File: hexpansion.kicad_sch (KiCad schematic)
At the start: 7 parts, among them J1 Hexpansion-Connector, J2 Conn_02x10_Odd_Even

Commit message: extract out hexpansion parts to custom library
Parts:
- J1: footprint tildagon:hexpansion-edge-connector -> parts:hexpansion-edge-connector; symbol tildagon:hexpansion-edge-connector -> parts:hexpansion-edge-connector
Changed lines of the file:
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@@
 	)
 	(symbol
-		(lib_id "tildagon:hexpansion-edge-connector")
+		(lib_id "parts:hexpansion-edge-connector")
 		(at 83.82 74.93 0)
 		(unit 1)
-		(exclude_from_sim yes)
+		(exclude_from_sim no)
 		(in_bom no)
 		(on_board yes)
@@
 			)
 		)
-		(property "Footprint" "tildagon:hexpansion-edge-connector"
+		(property "Footprint" "parts:hexpansion-edge-connector"
 			(at 83.82 77.47 0)
 			(effects

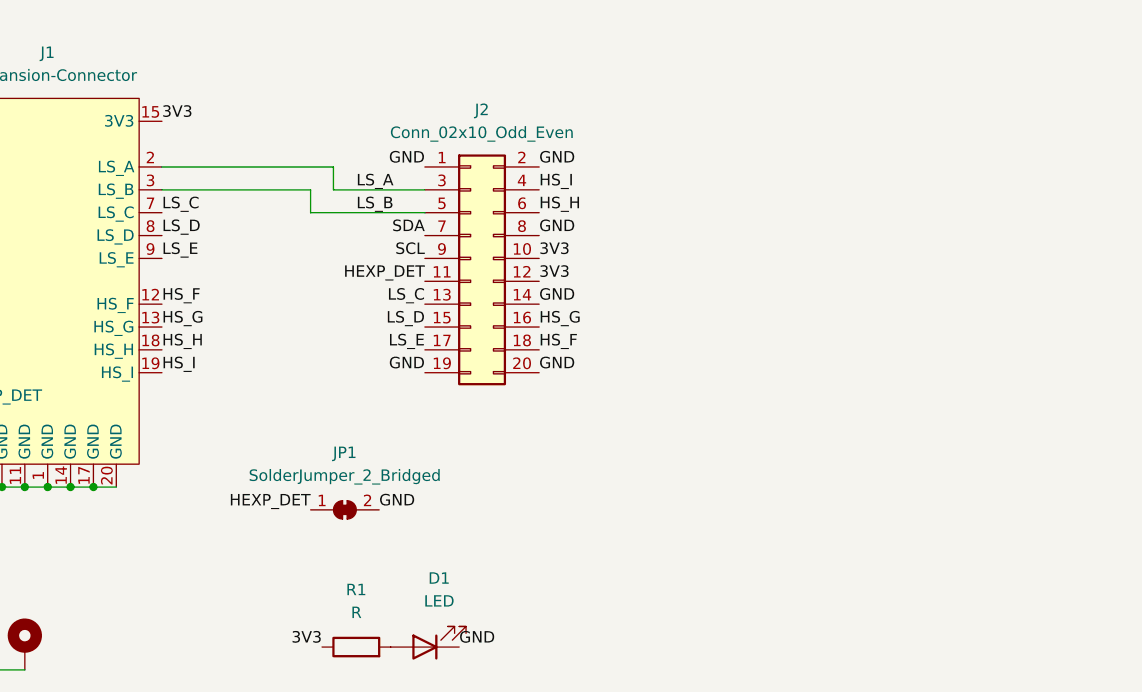
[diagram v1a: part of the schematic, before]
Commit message: add codec symbol
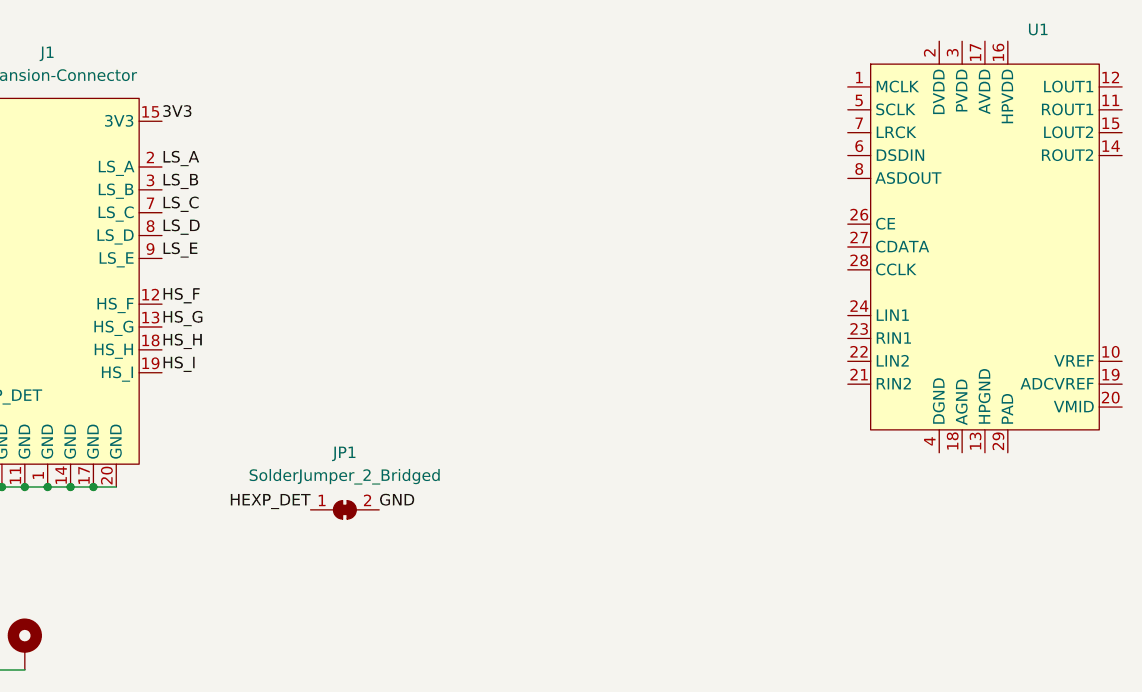
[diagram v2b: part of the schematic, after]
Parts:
- removed D1: LED, LED_SMD:LED_0805_2012Metric, symbol Device:LED
- removed J2: Conn_02x10_Odd_Even, Connector_PinHeader_2.54mm:PinHeader_2x10_P2.54mm_Vertical, symbol Connector_Generic:Conn_02x10_Odd_Even
- removed R1: R, Resistor_SMD:R_0603_1608Metric, symbol Device:R
- added U1: ~, symbol parts:ES8388

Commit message: rough sch
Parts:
- added C1, C10, C2, C4, C6, C8: 10 uF, symbol Device:C_Small
- added C11, C12, C21, C3, C5, C7, C9: 0.1 uF, symbol Device:C_Small
- added C13, C14: 47 uF, symbol Device:C_Small
- added C15, C16, C17, C18, C19, C20: 1 uF, symbol Device:C_Small
- added J2, J3, J4: AudioJack4, symbol Connector_Audio:AudioJack4
- added JP2: ADDR_LSB0, symbol Jumper:SolderJumper_3_Bridged12
- added R1, R2, R3, R4: 10, symbol Device:R_Small
- added R5, R6, R7, R8: 10k, symbol Device:R_Small
- added TP1: TestPoint, symbol Connector:TestPoint
- added U2, U3: 74LVC1G125, symbol 74xGxx:74LVC1G125
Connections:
- net 3V3 is gone; now on net +3.3V: J1.15 (3V3), J1.16 (3V3)
- net HS_F is gone; now on net MCLK: J1.12 (HS_F)
- net HS_G is gone; now on net SCLK: J1.13 (HS_G)
- net HS_H is gone; now on net LRCLK: J1.18 (HS_H)
- net GND: now also U1.13 (HPGND), U1.18 (AGND), U1.29 (PAD), U1.4 (DGND), C1.2, C10.2, C11.2, C12.2, C2.2, C21.2, C3.2, C4.2, C5.2, C6.2, C7.2, C8.2, C9.2, J2.R2, J3.R2, J3.S, J4.R2, J4.S, JP2.1 (A), R8.2, U2.3 (GND), U3.3 (GND)
- net SCL: now also U1.28 (CCLK), R6.2
- net SDA: now also U1.27 (CDATA), R5.2
- net MCLK: now reaches U1.1 (MCLK)
- net at U1.10 (VREF): now also C1.1
- net at U1.11 (ROUT1): now also C14.1
- net at U1.12 (LOUT1): now also C13.1
- net at U1.14 (ROUT2): now also C16.1
- net at U1.15 (LOUT2): now also C15.1
- net +3.3V: now reaches U1.16 (HPVDD)
- net +3.3V: now also U1.17 (AVDD), U1.2 (DVDD), U1.3 (PVDD), C10.1, C11.1, C12.1, C21.1, C6.1, C7.1, C8.1, C9.1, JP2.3 (B), R5.1, R6.1, R7.1, U2.5 (VCC), U3.5 (VCC)
- net at U1.19 (ADCVREF): now also C2.1, C3.1
- net at U1.20 (VMID): now also C4.1, C5.1
- net at U1.21 (RIN2): now also C20.2
- net at U1.22 (LIN2): now also C19.2
- net at U1.23 (RIN1): now also C18.2
- net at U1.24 (LIN1): now also C17.2
- net at U1.26 (CE): now also JP2.2 (C)
- net SCLK: now reaches U1.5 (SCLK)
- net DSDIN: now reaches U1.6 (DSDIN)
- net DSDIN: now also U3.4
- net LRCLK: now reaches U1.7 (LRCK)
- net ASDOUT: now reaches U1.8 (ASDOUT)
- net ASDOUT: now also U2.2
- net HS_I renamed I2S_DATA_SHARED
- net I2S_DATA_SHARED: now also U2.4, U3.2
- net LS_A renamed ~{MIC_EN}
- net ~{MIC_EN}: now also R7.2, U2.1
- net LS_B renamed ~{OUT_EN}
- net ~{OUT_EN}: now also R8.1, U3.1
- net LS_C: no longer names the net of J1.7 (LS_C)
- net LS_D: no longer names the net of J1.8 (LS_D)
- net LS_E: no longer names the net of J1.9 (LS_E)
- new net: C13.2, R1.1
- new net: C14.2, R2.1
- new net: C15.2, R4.1
- new net: C16.2, R3.1
- new net HP_L: J2.T, R1.2
- new net HP_R: J2.R1, R2.2
- new net LINEIN_L: C19.1, J4.T
- new net LINEIN_R: C20.1, J4.R1
- new net LINEOUT_L: J3.T, R4.2
- new net LINEOUT_R: J3.R1, R3.2
- new net MIC_L: C17.1, J2.S
- new net MIC_R: C18.1, TP1.1
- no-connect marks 0 -> 3
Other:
- note added: "AVDD"
- note added: "DVDD"
- note added: "HPVDD"
- note added: "PVDD"
- note added: "TODO do we want higher quality filtering?"
- note added: "lol the cheapest jack is a TRRS"
- note added: "todo verify pin ordering"
- note added: "xxx verify this is a MCLK capable pin???"
- moved on the sheet: J1, JP1, U1

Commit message: rough everything
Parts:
- added TP2: SCL, TestPoint:TestPoint_Pad_2.0x2.0mm, symbol Connector:TestPoint
- added TP3: SDA, TestPoint:TestPoint_Pad_2.0x2.0mm, symbol Connector:TestPoint
- added TP4: ASDOUT, TestPoint:TestPoint_Pad_1.0x1.0mm, symbol Connector:TestPoint
- added TP5: DSDIN, TestPoint:TestPoint_Pad_1.0x1.0mm, symbol Connector:TestPoint
- C1, C10, C2, C4, C6, C8: footprint (none) -> Capacitor_SMD:C_0603_1608Metric
- C11, C12, C21, C3, C5, C7, C9: footprint (none) -> Capacitor_SMD:C_0402_1005Metric
- C13, C14, C15, C16, C17, C18, C19, C20: footprint (none) -> Capacitor_SMD:C_1206_3216Metric
- J2, J3, J4: footprint (none) -> Connector_Audio:Jack_3.5mm_PJ320D_Horizontal
- JP2: footprint (none) -> Jumper:SolderJumper-3_P1.3mm_Bridged12_RoundedPad1.0x1.5mm
- R1, R2, R3, R4: footprint (none) -> Resistor_SMD:R_0603_1608Metric
- R5, R6, R7, R8: footprint (none) -> Resistor_SMD:R_0402_1005Metric
- TP1: footprint (none) -> TestPoint:TestPoint_Pad_2.0x2.0mm
- U1: footprint (none) -> parts:QFN-28-1EP_4x4mm_P0.45mm_EP2.6x2.6mm
- U2, U3: footprint (none) -> Package_TO_SOT_SMD:SOT-23-5
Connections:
- net ASDOUT: now also TP4.1
- net DSDIN: now also TP5.1
- net SCL: now also TP2.1
- net SDA: now also TP3.1
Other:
- note added: "FIXME THIS FOOTPRINT IS WRONG!"
- moved on the sheet: R8

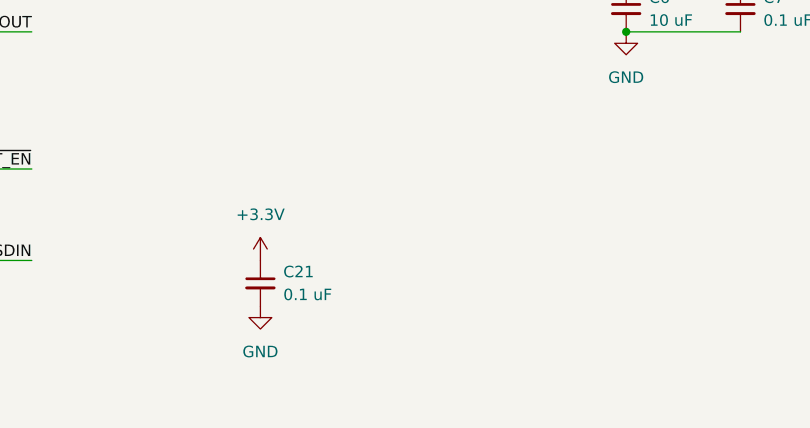
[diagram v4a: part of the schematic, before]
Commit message: rough route
purposely ignore extra gnd
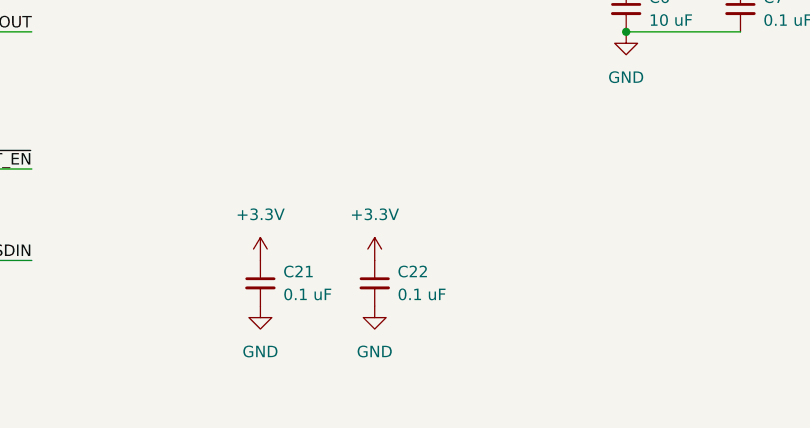
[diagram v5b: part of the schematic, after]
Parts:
- added C22: 0.1 uF, Capacitor_SMD:C_0402_1005Metric, symbol Device:C_Small
- J2, J3, J4: footprint Connector_Audio:Jack_3.5mm_PJ320D_Horizontal -> Connector_Audio:Jack_3.5mm_KoreanHropartsElec_PJ-320D-4A_Horizontal
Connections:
- net +3.3V: now also C22.1
- net GND: now also C22.2
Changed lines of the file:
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@@
 			)
 		)
-		(property "Footprint" "Connector_Audio:Jack_3.5mm_PJ320D_Horizontal"
+		(property "Footprint" "Connector_Audio:Jack_3.5mm_KoreanHropartsElec_PJ-320D-4A_Horizontal"
 			(at 182.88 25.4 0)
 			(effects
@@
 			)
 		)
-		(property "Footprint" "Connector_Audio:Jack_3.5mm_PJ320D_Horizontal"
+		(property "Footprint" "Connector_Audio:Jack_3.5mm_KoreanHropartsElec_PJ-320D-4A_Horizontal"
 			(at 144.78 25.4 0)
 			(effects
@@
 	)
 	(symbol
+		(lib_id "power:+3.3V")
+		(at 139.7 177.8 0)
+		(unit 1)
+		(exclude_from_sim no)
+		(in_bom yes)
+		(on_board yes)
+		(dnp no)
+		(fields_autoplaced yes)
+		(property "Reference" "#PWR028"
+			(at 139.7 181.61 0)
+			(effects
+				(font
+					(size 1.27 1.27)
+				)
+				(hide yes)
+			)
+		)
+		(property "Value" "+3.3V"
+			(at 139.7 172.72 0)
+			(effects
+				(font
+					(size 1.27 1.27)
+				)
+			)
+		)
+		(property "Footprint" ""
+			(at 139.7 177.8 0)
+			(effects
+				(font
+					(size 1.27 1.27)
+				)
+				(hide yes)
+			)
+		)
+		(property "Datasheet" ""
+			(at 139.7 177.8 0)
+			(effects
+				(font
+					(size 1.27 1.27)
+				)
+				(hide yes)
+			)
+		)
+		(property "Description" "Power symbol creates a global label with name \"+3.3V\""
+			(at 139.7 177.8 0)
+			(effects
+				(font
+					(size 1.27 1.27)
+				)
+				(hide yes)
+			)
+		)
+		(pin "1"
+		)
+		(instances
+			(project "hexpansion"
+				(path "/fb9bfa6e-c44d-469c-aa90-8ec28bcdf17f"
+					(reference "#PWR028")
+					(unit 1)
+				)
+			)
+		)
+	)
+	(symbol
 		(lib_id "power:GND")
 		(at 60.96 187.96 0)
@@
 	(symbol
 		(lib_id "Device:C_Small")
+		(at 139.7 180.34 0)
+		(unit 1)
+		(exclude_from_sim no)
+		(in_bom yes)
+		(on_board yes)
+		(dnp no)
+		(fields_autoplaced yes)
+		(property "Reference" "C22"
+			(at 142.24 179.0762 0)
+			(effects
+				(font
+					(size 1.27 1.27)
+				)
+				(justify left)
+			)
+		)
+		(property "Value" "0.1 uF"
+			(at 142.24 181.6162 0)
+			(effects
+				(font
+					(size 1.27 1.27)
+				)
+				(justify left)
+			)
+		)
+		(property "Footprint" "Capacitor_SMD:C_0402_1005Metric"
+			(at 139.7 180.34 0)
+			(effects
+				(font
+					(size 1.27 1.27)
+				)
+				(hide yes)
+			)
+		)
+		(property "Datasheet" "~"
+			(at 139.7 180.34 0)
+			(effects
+				(font
+					(size 1.27 1.27)
+				)
+				(hide yes)
+			)
+		)
+		(property "Description" "Unpolarized capacitor, small symbol"
+			(at 139.7 180.34 0)
+			(effects
+				(font
+					(size 1.27 1.27)
+				)
+				(hide yes)
+			)
+		)
+		(pin "1"
+		)
+		(pin "2"
+		)
+		(instances
+			(project "hexpansion"
+				(path "/fb9bfa6e-c44d-469c-aa90-8ec28bcdf17f"
+					(reference "C22")
+					(unit 1)
+				)
+			)
+		)
+	)
+	(symbol
+		(lib_id "Device:C_Small")
 		(at 111.76 109.22 90)
 		(unit 1)
@@
 			)
 		)
-		(property "Footprint" "Connector_Audio:Jack_3.5mm_PJ320D_Horizontal"
+		(property "Footprint" "Connector_Audio:Jack_3.5mm_KoreanHropartsElec_PJ-320D-4A_Horizontal"
 			(at 182.88 53.34 0)
 			(effects
@@
 					(unit 1)
 				)
+			)
+		)
+	)
+	(symbol
+		(lib_id "power:GND")
+		(at 139.7 182.88 0)
+		(unit 1)
+		(exclude_from_sim no)
+		(in_bom yes)
+		(on_board yes)
+		(dnp no)
+		(fields_autoplaced yes)
+		(property "Reference" "#PWR029"
+			(at 139.7 189.23 0)
+			(effects
+				(font
+					(size 1.27 1.27)
+				)
+				(hide yes)
+			)
+		)
+		(property "Value" "GND"
+			(at 139.7 187.96 0)
+			(effects
+				(font
+					(size 1.27 1.27)
+				)
+			)
+		)
+		(property "Footprint" ""
+			(at 139.7 182.88 0)
+			(effects
+				(font
+					(size 1.27 1.27)
+				)
+				(hide yes)
+			)
+		)
+		(property "Datasheet" ""
+			(at 139.7 182.88 0)
+			(effects
+				(font
+					(size 1.27 1.27)
+				)
+				(hide yes)
+			)
+		)
+		(property "Description" "Power symbol creates a global label with name \"GND\" , ground"
+			(at 139.7 182.88 0)
+			(effects
+				(font
+					(size 1.27 1.27)
+				)
+				(hide yes)
+			)
+		)
+		(pin "1"
+		)
+		(instances
+			(project "hexpansion"
+				(path "/fb9bfa6e-c44d-469c-aa90-8ec28bcdf17f"
+					(reference "#PWR029")
+					(unit 1)
+				)

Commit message: metadata
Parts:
- C1, C10, C2, C4, C6, C8: LCSC (none) -> C19702
- C11, C12, C21, C22, C3, C5, C7, C9: LCSC (none) -> C1525
- C13, C14: LCSC (none) -> C96123
- C15, C16, C17, C18, C19, C20: LCSC (none) -> C1848
- H1, H2, JP1, TP2, TP3: now left out of the parts list
- J2, J3, J4: LCSC (none) -> C431535
- R1, R2, R3, R4: LCSC (none) -> C22859
- R5, R6, R7, R8: LCSC (none) -> C25744
- TP1: value TestPoint -> MIC_R; now left out of the parts list
- U1: LCSC (none) -> C365736
- U2, U3: LCSC (none) -> C23654

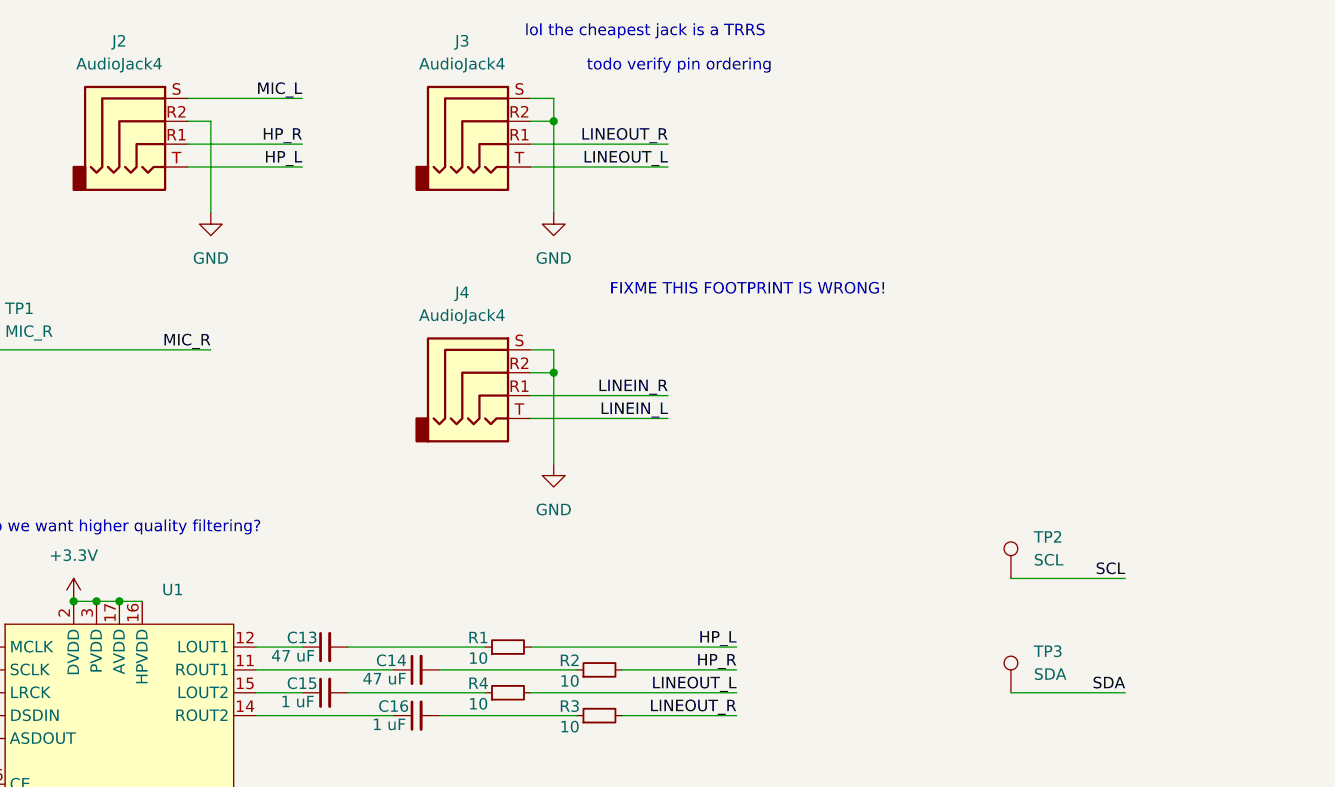
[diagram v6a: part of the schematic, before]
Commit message: doodles, fab layer cleanup
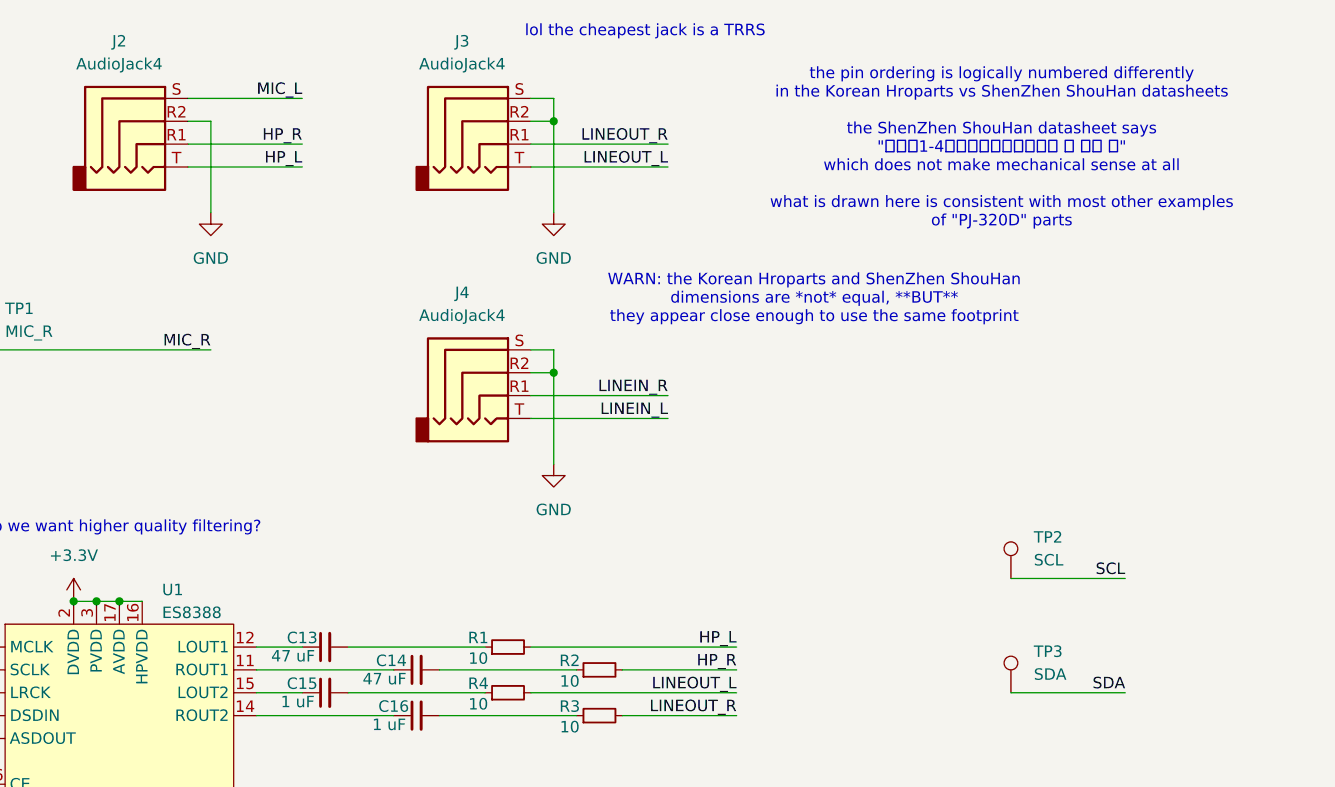
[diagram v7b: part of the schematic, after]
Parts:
- U1: value ~ -> ES8388
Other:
- note added: "WARN: the Korean Hroparts and ShenZhen ShouHan dimensions are *not* equal, **BUT** they appear close enough to use the same footprint"
- note added: "the pin ordering is logically numbered differently in the Korean Hroparts vs ShenZhen ShouHan datasheets the ShenZhen ShouHan datasheet says "插头第1-4节分别对应功能是：左 右 接地 唛" which does not make mechanical sense at all what is drawn here is consistent with most other examples of "PJ-320D" parts"
- note removed: "FIXME THIS FOOTPRINT IS WRONG!"
- note removed: "todo verify pin ordering"
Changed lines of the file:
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@@
 		)
 	)
-	(text "FIXME THIS FOOTPRINT IS WRONG!"
+	(text "WARN: the Korean Hroparts and ShenZhen ShouHan\ndimensions are *not* equal, **BUT**\nthey appear close enough to use the same footprint"
 		(exclude_from_sim no)
-		(at 212.09 44.196 0)
+		(at 219.456 45.212 0)
 		(effects
 			(font
@@
 		)
 	)
-	(text "todo verify pin ordering"
+	(text "the pin ordering is logically numbered differently\nin the Korean Hroparts vs ShenZhen ShouHan datasheets\n\nthe ShenZhen ShouHan datasheet says\n\"插头第1-4节分别对应功能是：左 右 接地 唛\"\nwhich does not make mechanical sense at all\n\nwhat is drawn here is consistent with most other examples\nof \"PJ-320D\" parts"
 		(exclude_from_sim no)
-		(at 204.47 19.304 0)
+		(at 240.284 28.448 0)
 		(effects
 			(font
@@
 			)
 		)
-		(property "Value" "~"
+		(property "Value" "ES8388"
 			(at 146.9741 80.01 0)
 			(effects

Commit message: generate fab outputs
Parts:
- TP4, TP5: now left out of the parts list
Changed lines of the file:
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@@
 		(unit 1)
 		(exclude_from_sim no)
-		(in_bom yes)
+		(in_bom no)
 		(on_board yes)
 		(dnp no)
@@
 		(unit 1)
 		(exclude_from_sim no)
-		(in_bom yes)
-		(on_board yes)
-		(dnp no)
+		(in_bom no)
+		(on_board yes)
+		(dnp no)
